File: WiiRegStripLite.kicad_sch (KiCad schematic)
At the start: 24 parts, among them U1 TLV62568DRL, U2 TLV62569DRL, U3 TLV62569DRL, U4 TLV62569DRL

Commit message: Integrated Power Strip, working on regulators and bq
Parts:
- added C1: 1uf, Capacitor_SMD:C_0603_1608Metric, symbol Device:C
- added C11: 4.7uf, Capacitor_SMD:C_0603_1608Metric, symbol Device:C
- added C12, C13, C14, C15, C26: 10uf, Capacitor_SMD:C_0805_2012Metric, symbol Device:C
- added C16, C17, C18, C19: 10uF, Capacitor_SMD:C_0805_2012Metric, symbol Device:C
- added C20, C21, C22, C23, C24, C25: 22uF, Capacitor_SMD:C_0805_2012Metric, symbol Device:C
- added C7: 0.047uf, Capacitor_SMD:C_0603_1608Metric, symbol Device:C
- added D1: B5819W, Diode_SMD:D_SOD-323, symbol Device:D_Schottky
- added J1, J2: Conn_01x04_Socket, Connector_PinHeader_2.54mm:PinHeader_1x04_P2.54mm_Horizontal, symbol Connector:Conn_01x04_Socket
- added L10, L6, L7, L8, L9: 1uH, Inductor_SMD:L_Vishay_IHLP-1212, symbol Device:L
- added L5: 2.2uh, Inductor_SMD:L_Wuerth_HCI-7030, symbol Device:L
- added R1: 261, Resistor_SMD:R_0603_1608Metric, symbol Device:R
- added R10, R11, R12, R13: 10k, Resistor_SMD:R_0603_1608Metric, symbol Device:R
- added R14: 66.5K, Resistor_SMD:R_0603_1608Metric, symbol Device:R
- added R15, R17, R19, R21: 100K, Resistor_SMD:R_0603_1608Metric, symbol Device:R
- added R16: 80k, Resistor_SMD:R_0603_1608Metric, symbol Device:R
- added R18: 414k, Resistor_SMD:R_0603_1608Metric, symbol Device:R_Small
- added R20: 470, Resistor_SMD:R_0603_1608Metric, symbol Device:R
- added R22: 124k, Resistor_SMD:R_0603_1608Metric, symbol Device:R_Small
- added R23: 100, Resistor_SMD:R_0603_1608Metric, symbol Device:R
- added R24: 732k, Resistor_SMD:R_0603_1608Metric, symbol Device:R
- added R25, R26: 100k, Resistor_SMD:R_0603_1608Metric, symbol Device:R
- added TP1: CHRG, TestPoint:TestPoint_Pad_1.5x1.5mm, symbol Connector:TestPoint
- added TP2: BAT+, TestPoint:TestPoint_Pad_1.5x1.5mm, symbol Connector:TestPoint
- added TP3: TestPoint, TestPoint:TestPoint_Pad_D1.0mm, symbol Connector:TestPoint
- added U10, U7, U8, U9: TLV62585DRL, Package_TO_SOT_SMD:SOT-563, symbol TLV62585DRL:TLV62585DRL
- added U11: ~, Package_TO_SOT_SMD:SOT-563, symbol New_Library:TPS61023DRLR
- added U5: BQ25895RTW, RVL-PMS HW2:BQ25895, symbol Battery_Management:BQ25895RTW
- added U6: ATtiny1616-M, Package_DFN_QFN:VQFN-20-1EP_3x3mm_P0.4mm_EP1.7x1.7mm, symbol MCU_Microchip_ATtiny:ATtiny1616-M
- C10, C2, C3, C4, C5, C6, C8, C9: footprint (none) -> Capacitor_SMD:C_0603_1608Metric
- L1, L2, L3, L4: footprint (none) -> Inductor_SMD:L_Vishay_IHLP-1212
- R2, R3, R4, R5, R6, R7, R8, R9: footprint (none) -> Resistor_SMD:R_0603_1608Metric
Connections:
- net 1V: now also C20.1, L6.2, R14.1
- net 1V35: now also C22.1, L8.2, R22.1
- net 3V: now also C23.1, L9.2, R18.1
- net EN: now also R26.2, U10.4 (EN), U7.4 (EN), U8.4 (EN), U9.4 (EN)
- net GND: now also C1.1, C11.2, C12.2, C13.1, C14.1, C15.1, C16.2, C17.2, C18.2, C19.2, C20.2, C21.2, C22.2, C23.2, C24.2, C25.2, C26.1, J1.1 (Pin_1), J2.2 (Pin_2), R1.1, R11.1, R15.2, R17.2, R19.2, R21.2, R25.2, U10.1 (GND), U11.4 (GND), U5.17 (PGND), U5.18 (PGND), U5.25 (PGND), U5.8 (OTG), U5.9 (~{CE}), U6.21 (GND), U6.3 (GND), U7.1 (GND), U8.1 (GND), U9.1 (GND)
- net VIN: now also C13.2, C14.2, C15.2, C16.1, C17.1, C18.1, C19.1, C26.2, J1.2 (Pin_2), L10.2, L5.1, R12.2, R13.1, TP3.1, U10.3 (VIN), U11.3 (VIN), U5.15 (SYS), U5.16 (SYS), U6.4 (VCC), U7.3 (VIN), U8.3 (VIN), U9.3 (VIN)
- new net: R26.1, U11.2 (EN)
- new net: R14.2, R15.1, U7.5 (FB)
- new net: R18.2, R21.1, U10.5 (FB)
- new net: R10.1, R11.2, U5.11 (TS)
- new net: C11.1, R10.2, U5.22 (REGN)
- new net: R16.2, R17.1, U8.5 (FB)
- new net: C1.2, TP1.1, U5.1 (VBUS)
- new net: R1.2, U5.10 (ILIM)
- new net: C12.1, TP2.1, U5.13 (BAT), U5.14 (BAT)
- new net: C7.1, U5.21 (BTST)
- new net: R24.2, R25.1, U11.1 (FB)
- new net: D1.1 (K), J1.3 (Pin_3)
- new net: D1.2 (A), J1.4 (Pin_4), R20.1
- new net: R19.1, R22.2, U9.5 (FB)
- new net 1V08: C21.1, L7.2, R16.1
- new net 5V: C24.1, C25.1, J2.3 (Pin_3), R24.1, U11.6 (VOUT)
- new net Inductor3vIn: L9.1, U10.2 (SW)
- new net L1v: L6.1, U7.2 (SW)
- new net L1v08: L7.1, U8.2 (SW)
- new net L1v35: L8.1, U9.2 (SW)
- new net L5v: L10.1, U11.5 (SW)
- new net LBQ: C7.2, L5.2, U5.19 (SW), U5.20 (SW)
- new net NeoPixelDIN: J2.4 (Pin_4), R23.1
- new net NeoPixelDO: J2.1 (Pin_1)
- new net PA1: U6.20 (PA1)
- new net PA2: U6.1 (PA2)
- new net PA3: U6.2 (PA3)
- new net PA4: U6.5 (PA4)
- new net PA5: U6.6 (PA5)
- new net PA6: U6.7 (PA6)
- new net PA7: R23.2, U6.8 (PA7)
- new net RX: U6.11 (PB3)
- new net SCL: R13.2, U5.5 (SCL), U6.14 (PB0)
- new net SDA: R12.1, U5.6 (SDA), U6.13 (PB1)
- new net TX: U6.12 (PB2)
- new net UPDI: R20.2, U6.19 (~{RESET}/PA0)
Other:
- moved on the sheet: C10, C2, C3, C4, C5, C6, C8, C9, L1, L2, L3, L4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

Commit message: More work
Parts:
- added J3: Fan, Connector_PinHeader_2.54mm:PinHeader_1x02_P2.54mm_Vertical, symbol Connector:Conn_01x02_Socket
- added R27: 10k, Resistor_SMD:R_0603_1608Metric, symbol Device:R
- added TH1: 10k, Resistor_SMD:R_0603_1608Metric, symbol Device:Thermistor_NTC
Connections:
- net GND: now also J3.1 (Pin_1), TH1.2
- net PA1: now also R27.1, TH1.1
- net PA4: now also J3.2 (Pin_2)
- net VIN: now also R27.2

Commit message: Final Design
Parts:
- J1: footprint Connector_PinHeader_2.54mm:PinHeader_1x04_P2.54mm_Horizontal -> Connector_PinHeader_2.54mm:PinHeader_1x04_P2.54mm_Vertical
- J2: footprint Connector_PinHeader_2.54mm:PinHeader_1x04_P2.54mm_Horizontal -> Connector_PinHeader_2.54mm:PinHeader_1x05_P2.54mm_Vertical; symbol Connector:Conn_01x04_Socket -> Connector:Conn_01x05_Socket
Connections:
- net NeoPixelDO is gone; now on net GND: J2.1 (Pin_1)
- net PA2 is gone; now on net EN: U6.1 (PA2)
- net 5V: now also J2.2 (Pin_2); no longer J2.3 (Pin_3)
- net GND: no longer J2.2 (Pin_2)
- net NeoPixelDIN: no longer J2.4 (Pin_4)
- net RX: now also J2.4 (Pin_4)
- net TX: now also J2.3 (Pin_3)
- net PA5 renamed BTN
- net BTN: now also J2.5 (Pin_5)

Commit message: Gerber gen and new ibom
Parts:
- U11: value ~ -> TPS61023DRLR
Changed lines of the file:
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@@
 			)
 		)
-		(property "Value" "~"
+		(property "Value" "TPS61023DRLR"
 			(at 165.354 111.76 0)
 			(effects

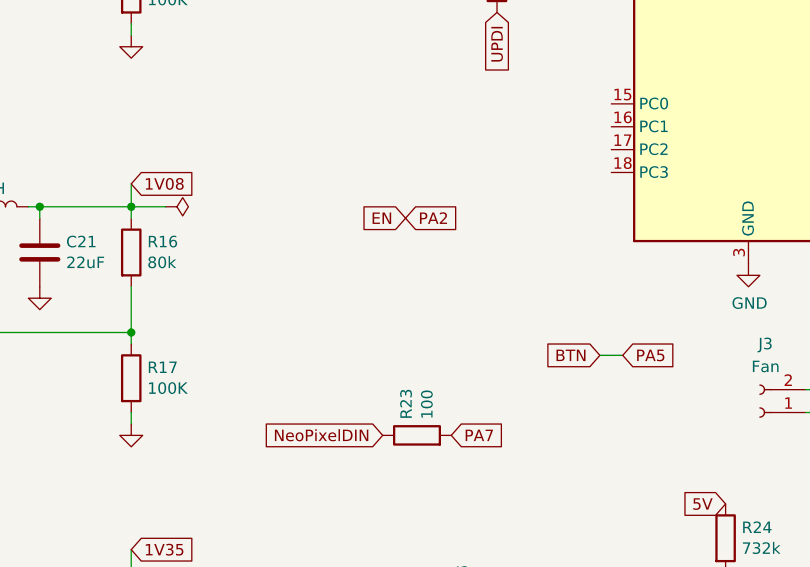
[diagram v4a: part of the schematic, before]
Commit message: More edits
Rounded edges, moved traces, added EN pull down resistor
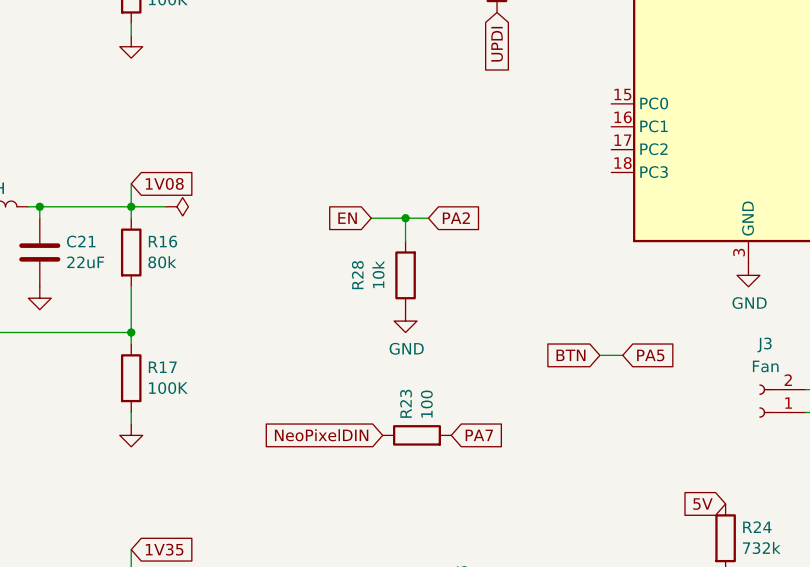
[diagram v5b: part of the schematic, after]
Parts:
- added R28: 10k, Resistor_SMD:R_0603_1608Metric, symbol Device:R
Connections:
- net EN: now also R28.2
- net GND: now also R28.1
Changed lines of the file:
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@@
 	)
 	(junction
+		(at 109.22 78.74)
+		(diameter 0)
+		(color 0 0 0 0)
+	)
+	(junction
 		(at 68.58 34.29)
 		(diameter 0)
@@
 	(wire
 		(pts
+			(xy 109.22 78.74) (xy 111.76 78.74)
+		)
+		(stroke
+			(width 0)
+			(type default)
+		)
+	)
+	(wire
+		(pts
 			(xy 116.84 35.56) (xy 116.84 40.64)
 		)
@@
 	(wire
 		(pts
+			(xy 105.41 78.74) (xy 109.22 78.74)
+		)
+		(stroke
+			(width 0)
+			(type default)
+		)
+	)
+	(wire
+		(pts
 			(xy 153.67 100.33) (xy 156.21 100.33)
 		)
@@
 		)
 	)
+	(wire
+		(pts
+			(xy 109.22 78.74) (xy 109.22 81.28)
+		)
+		(stroke
+			(width 0)
+			(type default)
+		)
+	)
 	(rectangle
 		(start -171.45 43.18)
@@
 	(global_label "EN"
 		(shape input)
-		(at 109.22 78.74 180)
+		(at 105.41 78.74 180)
 		(fields_autoplaced yes)
 		(effects
@@
 		)
 		(property "Intersheetrefs" "${INTERSHEET_REFS}"
-			(at 103.7553 78.74 0)
+			(at 99.9453 78.74 0)
 			(effects
 				(font
@@
 	(global_label "PA2"
 		(shape input)
-		(at 109.22 78.74 0)
+		(at 111.76 78.74 0)
 		(fields_autoplaced yes)
 		(effects
@@
 		)
 		(property "Intersheetrefs" "${INTERSHEET_REFS}"
-			(at 115.7733 78.74 0)
+			(at 118.3133 78.74 0)
 			(effects
 				(font
@@
 	)
 	(symbol
+		(lib_id "power:GND")
+		(at 109.22 88.9 0)
+		(unit 1)
+		(exclude_from_sim no)
+		(in_bom yes)
+		(on_board yes)
+		(dnp no)
+		(property "Reference" "#PWR031"
+			(at 109.22 95.25 0)
+			(effects
+				(font
+					(size 1.27 1.27)
+				)
+				(hide yes)
+			)
+		)
+		(property "Value" "GND"
+			(at 109.347 93.2942 0)
+			(effects
+				(font
+					(size 1.27 1.27)
+				)
+			)
+		)
+		(property "Footprint" ""
+			(at 109.22 88.9 0)
+			(effects
+				(font
+					(size 1.27 1.27)
+				)
+				(hide yes)
+			)
+		)
+		(property "Datasheet" ""
+			(at 109.22 88.9 0)
+			(effects
+				(font
+					(size 1.27 1.27)
+				)
+				(hide yes)
+			)
+		)
+		(property "Description" ""
+			(at 109.22 88.9 0)
+			(effects
+				(font
+					(size 1.27 1.27)
+				)
+				(hide yes)
+			)
+		)
+		(pin "1"
+		)
+		(instances
+			(project "WiiRegStripLite"
+				(path "/fea92c4c-2e49-45e9-911c-7a64315d44ed"
+					(reference "#PWR031")
+					(unit 1)
+				)
+			)
+		)
+	)
+	(symbol
 		(lib_id "Device:C_Small")
 		(at -107.95 66.04 0)
@@
 					(unit 1)
 				)
+			)
+		)
+	)
+	(symbol
+		(lib_id "Device:R")
+		(at 109.22 85.09 180)
+		(unit 1)
+		(exclude_from_sim no)
+		(in_bom yes)
+		(on_board yes)
+		(dnp no)
+		(property "Reference" "R28"
+			(at 103.9622 85.09 90)
+			(effects
+				(font
+					(size 1.27 1.27)
+				)
+			)
+		)
+		(property "Value" "10k"
+			(at 106.2736 85.09 90)
+			(effects
+				(font
+					(size 1.27 1.27)
+				)
+			)
+		)
+		(property "Footprint" "Resistor_SMD:R_0603_1608Metric"
+			(at 110.998 85.09 90)
+			(effects
+				(font
+					(size 1.27 1.27)
+				)
+				(hide yes)
+			)
+		)
+		(property "Datasheet" "~"
+			(at 109.22 85.09 0)
+			(effects
+				(font
+					(size 1.27 1.27)
+				)
+				(hide yes)
+			)
+		)
+		(property "Description" ""
+			(at 109.22 85.09 0)
+			(effects
+				(font
+					(size 1.27 1.27)
+				)
+				(hide yes)
+			)
+		)
+		(pin "1"
+		)
+		(pin "2"
+		)
+		(instances
+			(project "WiiRegStripLite"
+				(path "/fea92c4c-2e49-45e9-911c-7a64315d44ed"
+					(reference "R28")
+					(unit 1)
+				)

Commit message: A LOT of firmware work
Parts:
- removed C10, C3, C5, C6: 22uF, Capacitor_SMD:C_0603_1608Metric, symbol Device:C_Small
- removed C2, C4, C8, C9: 4.7uF, Capacitor_SMD:C_0603_1608Metric, symbol Device:C_Small
- removed L1: 1uH, Inductor_SMD:L_Vishay_IHLP-1212, symbol Device:L
- removed L2, L3, L4: 2.2uH, Inductor_SMD:L_Vishay_IHLP-1212, symbol Device:L
- removed R2: 124k, Resistor_SMD:R_0603_1608Metric, symbol Device:R_Small
- removed R3, R5, R7, R9: 100k, Resistor_SMD:R_0603_1608Metric, symbol Device:R_Small
- removed R4: 414k, Resistor_SMD:R_0603_1608Metric, symbol Device:R_Small
- removed R6, R8: 66.5k, Resistor_SMD:R_0603_1608Metric, symbol Device:R_Small
- removed U1: TLV62568DRL, Package_TO_SOT_SMD:SOT-563, symbol Regulator_Switching:TLV62568DRL
- removed U2, U3, U4: TLV62569DRL, Package_TO_SOT_SMD:SOT-563, symbol Regulator_Switching:TLV62569DRL
- added TP4: U10, TestPoint:TestPoint_Pad_D1.0mm, symbol Connector:TestPoint
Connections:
- net PC0: now reaches U6.15 (PC0)
- net PC0: now also TP4.1
- net PA3: no longer names the net of U6.2 (PA3)
